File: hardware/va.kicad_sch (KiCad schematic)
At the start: 17 parts, among them U14 74AUC2G32, U16 SN74LVC245AN, U25 SN74LVC8T245, U26 SN74LVC2T45DCUR, U27 SN74LVC1T45DBV, U28 74AHC1G08

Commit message: Moved connection to external connections
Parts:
- added unit 3 of U14
- U25: footprint (none) -> Package_DIP:DIP-20_W7.62mm
- U28: footprint (none) -> Package_TO_SOT_SMD:SOT-23-5
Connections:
- net +3.3V: now also U14.8 (VCC)
- net GND: now also U14.4 (GND)
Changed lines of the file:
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@@
+	)
+	(symbol
+		(lib_id "74xGxx:74AUC2G32")
+		(at 29.21 62.23 0)
+		(unit 3)
+		(exclude_from_sim no)
+		(in_bom yes)
+		(on_board yes)
+		(dnp no)
+		(fields_autoplaced yes)
+		(property "Reference" "U14"
+			(at 35.56 60.9599 0)
+			(effects
+				(font
+					(size 1.27 1.27)
+				)
+				(justify left)
+			)
+		)
+		(property "Value" "74AUC2G32"
+			(at 35.56 63.4999 0)
+			(effects
+				(font
+					(size 1.27 1.27)
+				)
+				(justify left)
+			)
+		)
+		(property "Footprint" "Package_SO:SSOP-8_2.95x2.8mm_P0.65mm"
+			(at 29.21 62.23 0)
+			(effects
+				(font
+					(size 1.27 1.27)
+				)
+				(hide yes)
+			)
+		)
+		(property "Datasheet" "http://www.ti.com/lit/sg/scyt129e/scyt129e.pdf"
+			(at 29.21 62.23 0)
+			(effects
+				(font
+					(size 1.27 1.27)
+				)
+				(hide yes)
+			)
+		)
+		(property "Description" "Dual OR Gate, Low-Voltage CMOS"
+			(at 29.21 62.23 0)
+			(effects
+				(font
+					(size 1.27 1.27)
+				)
+				(hide yes)
+			)
+		)
+		(pin "6"
+		)
+		(pin "5"
+		)
+		(pin "2"
+		)
+		(pin "1"
+		)
+		(pin "7"
+		)
+		(pin "8"
+		)
+		(pin "4"
+		)
+		(pin "3"
+		)
+		(instances
+			(project "Lambda One"
+				(path "/73ea9964-373f-4fdc-b03e-f532cf836c0d/17c7449d-caad-4fd1-a972-8af3d0bf5f54"
+					(reference "U14")
+					(unit 3)
+				)
+			)
+		)
 	)
 	(symbol
@@
 			)
 		)
-		(property "Footprint" ""
+		(property "Footprint" "Package_TO_SOT_SMD:SOT-23-5"
 			(at 80.01 111.76 0)
 			(effects
@@
 	)
 	(symbol
+		(lib_id "power:GND")
+		(at 29.21 72.39 0)
+		(unit 1)
+		(exclude_from_sim no)
+		(in_bom yes)
+		(on_board yes)
+		(dnp no)
+		(fields_autoplaced yes)
+		(property "Reference" "#PWR075"
+			(at 29.21 78.74 0)
+			(effects
+				(font
+					(size 1.27 1.27)
+				)
+				(hide yes)
+			)
+		)
+		(property "Value" "GND"
+			(at 29.21 77.47 0)
+			(effects
+				(font
+					(size 1.27 1.27)
+				)
+			)
+		)
+		(property "Footprint" ""
+			(at 29.21 72.39 0)
+			(effects
+				(font
+					(size 1.27 1.27)
+				)
+				(hide yes)
+			)
+		)
+		(property "Datasheet" ""
+			(at 29.21 72.39 0)
+			(effects
+				(font
+					(size 1.27 1.27)
+				)
+				(hide yes)
+			)
+		)
+		(property "Description" "Power symbol creates a global label with name \"GND\" , ground"
+			(at 29.21 72.39 0)
+			(effects
+				(font
+					(size 1.27 1.27)
+				)
+				(hide yes)
+			)
+		)
+		(pin "1"
+		)
+		(instances
+			(project "Lambda One"
+				(path "/73ea9964-373f-4fdc-b03e-f532cf836c0d/17c7449d-caad-4fd1-a972-8af3d0bf5f54"
+					(reference "#PWR075")
+					(unit 1)
+				)
+			)
+		)
+	)
+	(symbol
 		(lib_id "power:+3.3V")
 		(at 29.21 162.56 0)
@@
 			)
 		)
-		(property "Footprint" ""
+		(property "Footprint" "Package_DIP:DIP-20_W7.62mm"
 			(at 184.15 152.4 0)
 			(effects
@@
 					(unit 1)
 				)
+			)
+		)
+	)
+	(symbol
+		(lib_id "power:+3.3V")
+		(at 29.21 52.07 0)
+		(unit 1)
+		(exclude_from_sim no)
+		(in_bom yes)
+		(on_board yes)
+		(dnp no)
+		(fields_autoplaced yes)
+		(property "Reference" "#PWR074"
+			(at 29.21 55.88 0)
+			(effects
+				(font
+					(size 1.27 1.27)
+				)
+				(hide yes)
+			)
+		)
+		(property "Value" "+3.3V"
+			(at 29.21 46.99 0)
+			(effects
+				(font
+					(size 1.27 1.27)
+				)
+			)
+		)
+		(property "Footprint" ""
+			(at 29.21 52.07 0)
+			(effects
+				(font
+					(size 1.27 1.27)
+				)
+				(hide yes)
+			)
+		)
+		(property "Datasheet" ""
+			(at 29.21 52.07 0)
+			(effects
+				(font
+					(size 1.27 1.27)
+				)
+				(hide yes)
+			)
+		)
+		(property "Description" "Power symbol creates a global label with name \"+3.3V\""
+			(at 29.21 52.07 0)
+			(effects
+				(font
+					(size 1.27 1.27)
+				)
+				(hide yes)
+			)
+		)
+		(pin "1"
+		)
+		(instances
+			(project "Lambda One"
+				(path "/73ea9964-373f-4fdc-b03e-f532cf836c0d/17c7449d-caad-4fd1-a972-8af3d0bf5f54"
+					(reference "#PWR074")
+					(unit 1)
+				)

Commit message: PCD DESIGN
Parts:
- renumbered U16 to DB5V1
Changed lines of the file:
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@@
 		(on_board yes)
 		(dnp no)
-		(property "Reference" "U16"
+		(property "Reference" "DB5V1"
 			(at 123.698 51.054 0)
 			(effects
@@
 			(project "Lambda One"
 				(path "/73ea9964-373f-4fdc-b03e-f532cf836c0d/17c7449d-caad-4fd1-a972-8af3d0bf5f54"
-					(reference "U16")
+					(reference "DB5V1")
 					(unit 1)
 				)

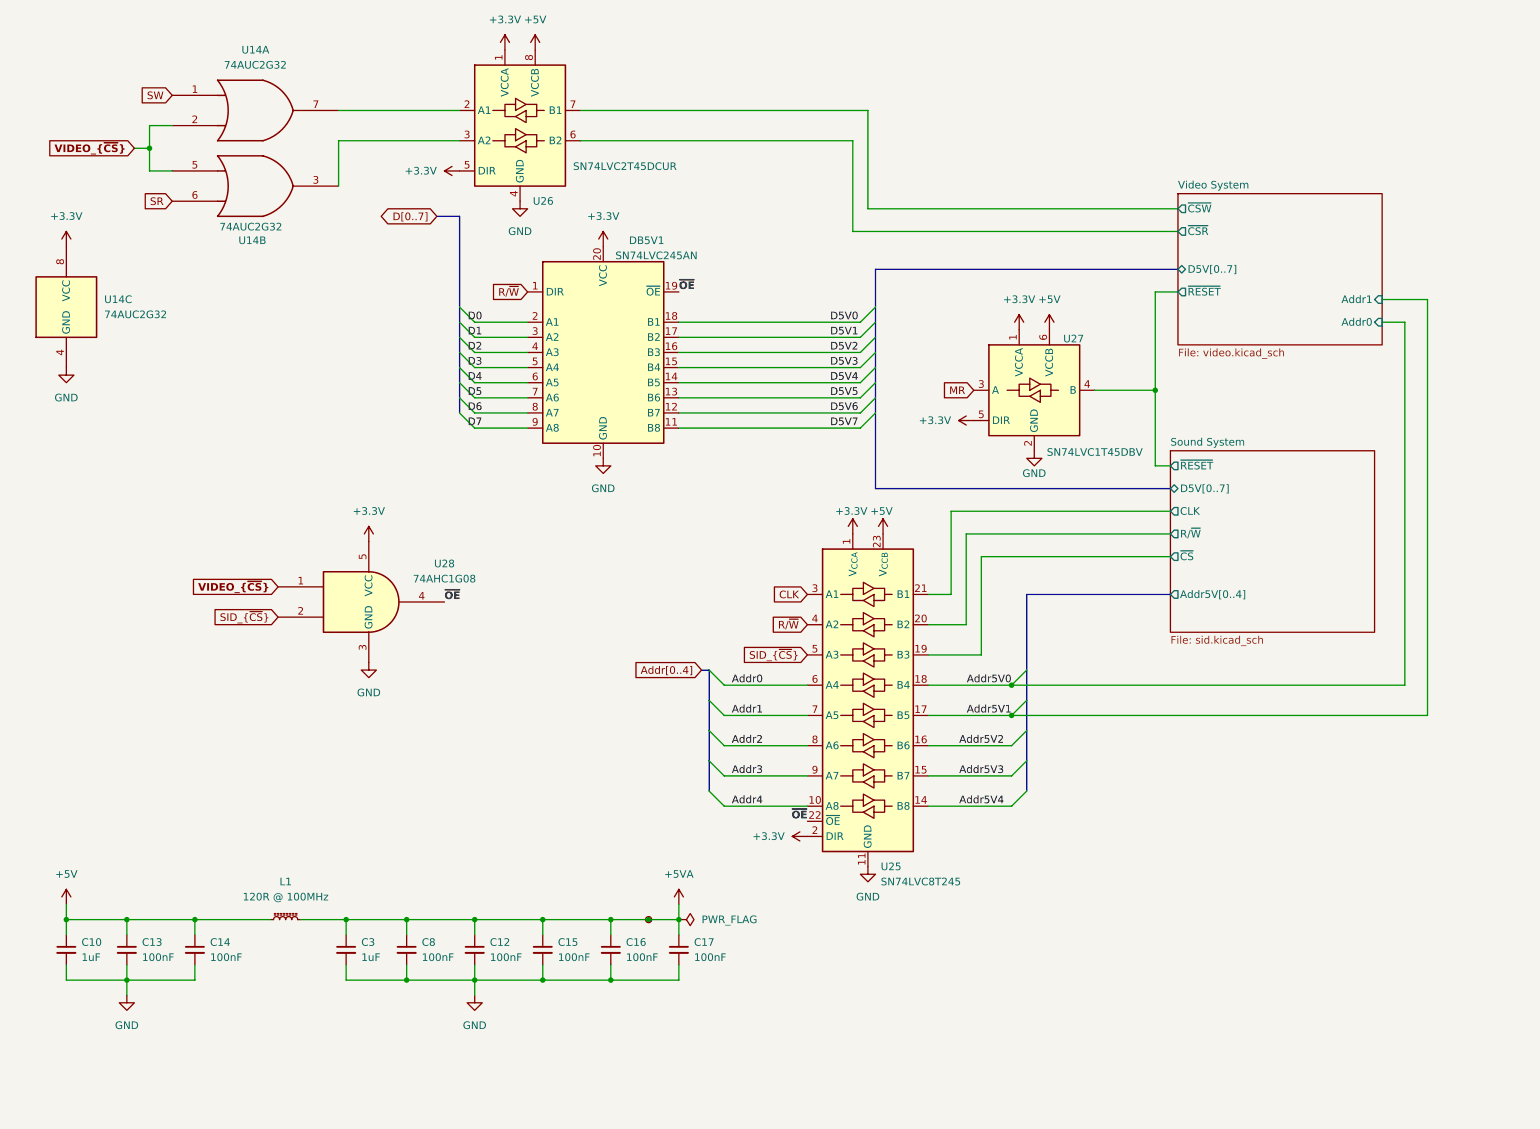
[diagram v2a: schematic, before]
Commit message: Removed old VPU
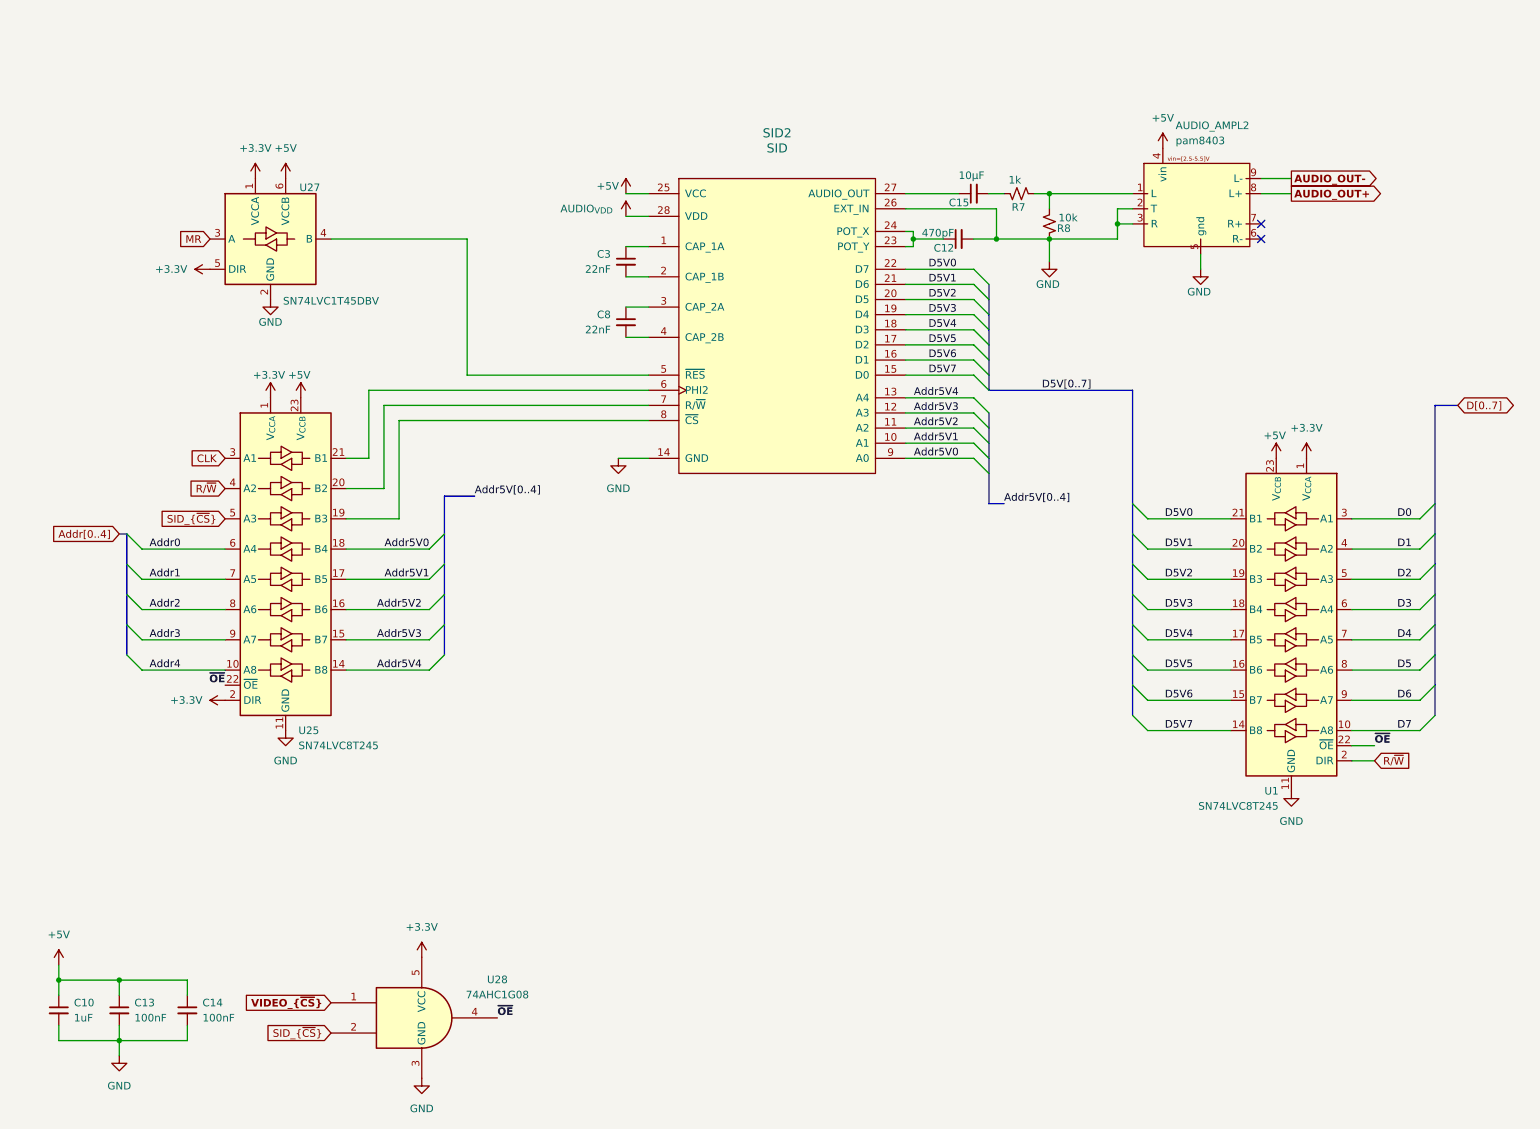
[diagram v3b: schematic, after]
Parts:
- removed C16, C17: 100nF, Capacitor_SMD:C_0603_1608Metric, symbol Device:C_Small
- removed DB5V1: SN74LVC245AN, Package_DIP:DIP-20_W7.62mm, symbol Logic_LevelTranslator:SN74LVC245APW
- removed L1: 120R @ 100MHz, Inductor_SMD:L_0603_1608Metric, symbol Device:L_Ferrite_Small
- removed TP1: TestPoint_Small, TestPoint:TestPoint_Pad_D1.5mm, symbol Connector:TestPoint_Small
- removed U14: 74AUC2G32, Package_SO:SSOP-8_2.95x2.8mm_P0.65mm, symbol 74xGxx:74AUC2G32
- removed U26: SN74LVC2T45DCUR, Package_SO:VSSOP-8_2.3x2mm_P0.5mm, symbol Logic_LevelTranslator:SN74LVC2T45DCUR
- added AUDIO_AMPL2: pam8403, pam8403:pam8403, symbol pam8403:pam8403
- added R7: 1k, Resistor_SMD:R_0603_1608Metric, symbol Device:R_Small_US
- added R8: 10k, Resistor_SMD:R_0603_1608Metric, symbol Device:R_Small_US
- added SID2: SID, Package_DIP:DIP-28_W15.24mm_Socket, symbol SID:MOS6581/6582/8580SID
- added U1: SN74LVC8T245, Package_DIP:DIP-20_W7.62mm, symbol Logic_LevelTranslator:SN74LVC8T245
- C12: value 100nF -> 470pF
- C15: value 100nF -> 10µF
- C3: value 1uF -> 22nF; PartNumber CL10A105KB8NNNC -> CL10B104KB8NNNC
- C8: value 100nF -> 22nF
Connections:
- net +3.3V: now also U1.1 (V_{CCA})
- net +5V: now also AUDIO_AMPL2.4 (vin), SID2.25 (VCC), U1.23 (V_{CCB}), U1.24 (V_{CCB})
- net Addr5V0: now also SID2.9 (A0)
- net Addr5V1: now also SID2.10 (A1)
- net Addr5V2: now also SID2.11 (A2)
- net Addr5V3: now also SID2.12 (A3)
- net Addr5V4: now also SID2.13 (A4)
- net D0: now also U1.3 (A1)
- net D1: now also U1.4 (A2)
- net D2: now also U1.5 (A3)
- net D3: now also U1.6 (A4)
- net D4: now also U1.7 (A5)
- net D5: now also U1.8 (A6)
- net D5V0: now also SID2.22 (D7), U1.21 (B1)
- net D5V1: now also SID2.21 (D6), U1.20 (B2)
- net D5V2: now also SID2.20 (D5), U1.19 (B3)
- net D5V3: now also SID2.19 (D4), U1.18 (B4)
- net D5V4: now also SID2.18 (D3), U1.17 (B5)
- net D5V5: now also SID2.17 (D2), U1.16 (B6)
- net D5V6: now also SID2.16 (D1), U1.15 (B7)
- net D5V7: now also SID2.15 (D0), U1.14 (B8)
- net D6: now also U1.9 (A7)
- net D7: now also U1.10 (A8)
- net GND: now also AUDIO_AMPL2.2 (T), AUDIO_AMPL2.3 (R), AUDIO_AMPL2.5 (gnd), R8.2, SID2.14 (GND), SID2.26 (EXT_IN), U1.11 (GND), U1.12 (GND), U1.13 (GND); no longer C15.2, C3.2, C8.2
- net R/~{W}: now also U1.2 (DIR)
- net ~{OE}: now also U1.22 (~{OE})
- removed net +5VA: C12.1, C15.1, C3.1, C8.1
- net Sound System/CLK: no longer names the net of U25.21 (B1)
- net Sound System/CLK: now also SID2.6 (PHI2)
- net Sound System/R/~{W}: no longer names the net of U25.20 (B2)
- net Sound System/R/~{W}: now also SID2.7 (R/~{W})
- net Sound System/~{CS}: no longer names the net of U25.19 (B3)
- net Sound System/~{CS}: now also SID2.8 (~{CS})
- net Sound System/~{RESET}: no longer names the net of U27.4 (B)
- net Sound System/~{RESET}: now also SID2.5 (~{RES})
- new net: AUDIO_AMPL2.1 (L), R7.1, R8.1
- new net: C3.1, SID2.1 (CAP_1A)
- new net: C3.2, SID2.2 (CAP_1B)
- new net: C15.2, R7.2
- new net: C12.1, SID2.23 (POT_Y), SID2.24 (POT_X)
- new net: C15.1, SID2.27 (AUDIO_OUT)
- new net: C8.1, SID2.3 (CAP_2A)
- new net: C8.2, SID2.4 (CAP_2B)
- new net AUDIO_OUT+: AUDIO_AMPL2.8 (L+)
- new net AUDIO_OUT-: AUDIO_AMPL2.9 (L-)
- new net AUDIO_{VDD}: SID2.28 (VDD)
- no-connect marks 0 -> 2
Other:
- removed sheet Sound System
- removed sheet Video System
- title: (none) -> Lambda One - Audio System
- moved on the sheet: C10, C13, C14, U25, U27, U28

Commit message: Removed old VPU
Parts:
- removed U28: 74AHC1G08, Package_TO_SOT_SMD:SOT-23-5, symbol 74xGxx:74AHC1G08
- added C34: 470µF, Fuse:Fuse_Bourns_MF-RG1000, symbol Device:C_Small
- U1, U25: footprint Package_DIP:DIP-20_W7.62mm -> Package_SO:SSOP-24_3.9x8.7mm_P0.635mm
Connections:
- net +5V: now also C34.1
- net GND: now also U25.22 (~{OE}), C34.2
- net R/~{W}: no longer U1.2 (DIR)
- net SID_{~{CS}}: now also U1.22 (~{OE})
- removed net ~{OE}: U1.22 (~{OE}), U25.22 (~{OE})
- new net ~{R}/W: U1.2 (DIR)
